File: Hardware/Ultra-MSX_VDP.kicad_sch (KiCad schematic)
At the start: 4 parts, among them J3 Ultra-VDP-daughter

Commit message: Started fixing many small issues.
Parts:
- added C12: C_GRM21BR71A106KA73K, Capacitor_SMD:C_0805_2012Metric_Pad1.18x1.45mm_HandSolder, symbol LRJ-parts:C_GRM21BR71A106KA73K
- added J12: Amphenol_L77HDE15SOL2, LRJ:Amphenol_L77HDE15SOL2, symbol LRJ-parts:Amphenol_L77HDE15SOL2
- added J13: Conn_NREC004, Connector_PinHeader_2.54mm:PinHeader_1x06_P2.54mm_Vertical_SMD_Pin1Right, symbol LRJ-parts:Conn_NREC006
- added R43: R_ERJ-3GEYJ105V, Resistor_SMD:R_0603_1608Metric, symbol LRJ-parts:R_ERJ-3GEYJ105V
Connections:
- net GNDA is gone; now on net GND: J3.47
- net +5V: now also C12.1, J12.9 (DC_5V)
- net BOUT: now also J12.3 (BLUE)
- net GND: now also C12.2, J12.10 (Sync_Ret/GND), J12.5 (GNDD), J12.6 (GNDr), J12.7 (GNDg), J12.8 (GNDb), J13.6 (Pin_6), R43.1
- net GOUT: now also J12.2 (GREEN)
- net HSYNC: now also J12.13 (HSync)
- net ROUT: now also J12.1 (RED)
- net TCK_VDP: now also J13.2 (Pin_2)
- net TDI_VDP: now also J13.3 (Pin_3)
- net TDO_VDP: now also J13.1 (Pin_1)
- net TMS_VDP: now also J13.4 (Pin_4)
- net VSYNC: now also J12.14 (VSync)
- new net: J12.11, J12.12, J12.15, J12.SH, R43.2
- new net +3.3V: J13.5 (Pin_5)
- new net VID_ID: J12.4 (ID_Bit2)
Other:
- note added: "Addressing"
- note added: "Clocks VDP"
- note added: "Data Bus"
- note added: "JTAG"
- note added: "JTAG connector"
- note added: "Only used with an F18A VDP."
- note added: "Video Signals"
- note removed: "Memory-suggestions: ----------------------- Modern ---- IS42S16100H IS45S16100H Legacy ----"
- note removed: "Off-limits names ---- Headers: J1 J2 J3 J4 J5 J6 J7 J11 Chips: U3 U6 U14 Crystals: Y1 Y3 Caps: C1 C2 C3 C9 C10 C11 C12 C13 C14 C15 C16 C73 Resistors: R12 R16 R17"
- note removed: "VTO - voltage Controlled Oscillator -------- Frequencies needed: 25.175 MHz 4.43361875 MHz 3.579545 MHz"

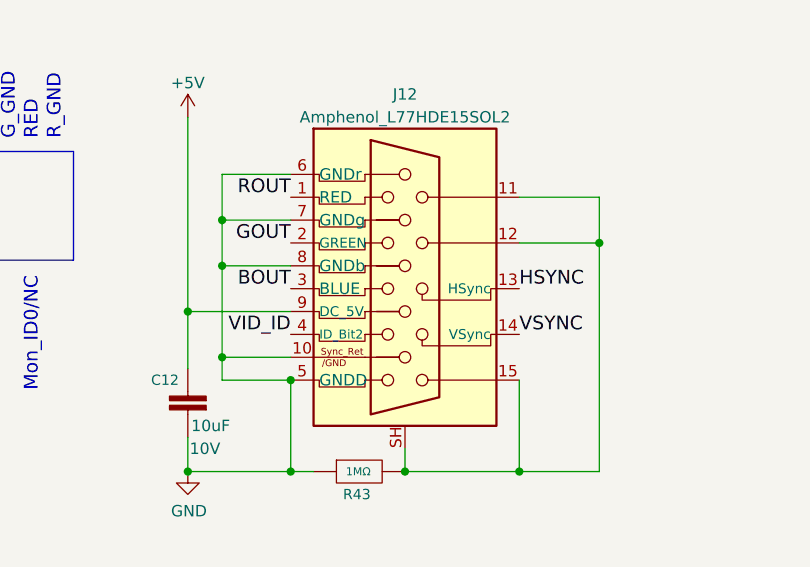
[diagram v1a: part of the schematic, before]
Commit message: Updated the readme, silenced multiple errors in Kicad regarding simulation-files.
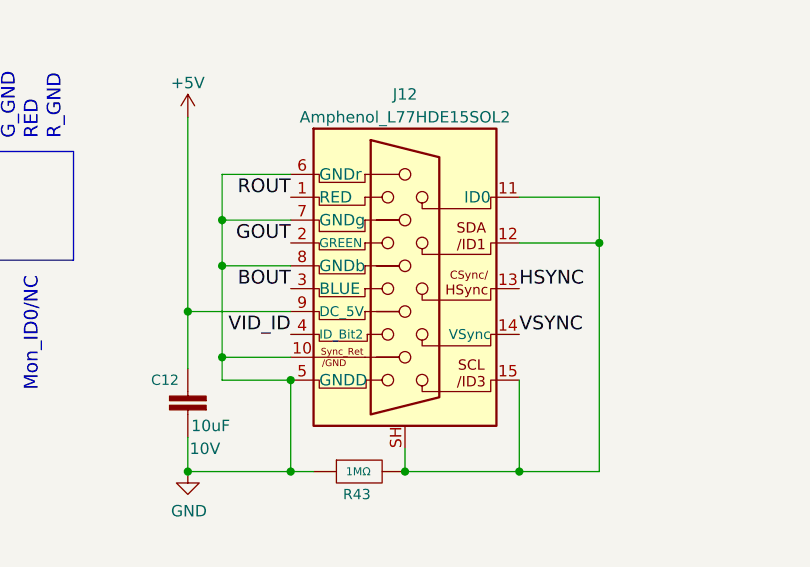
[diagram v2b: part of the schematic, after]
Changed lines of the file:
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@@
+      (effects (font (size 1.27 1.27)) hide)
+    )
+    (property "Sim.Enable" "0" (at 314.96 44.45 0)
       (effects (font (size 1.27 1.27)) hide)
     )
@@
     )
     (property "Datasheet" "~" (at 53.467 38.608 0)
+      (effects (font (size 1.27 1.27)) hide)
+    )
+    (property "Sim.Enable" "0" (at 53.34 91.44 0)
       (effects (font (size 1.27 1.27)) hide)
     )
@@
       (effects (font (size 1.27 1.27)) hide)
     )
+    (property "Sim.Enable" "0" (at 120.65 59.69 0)
+      (effects (font (size 1.27 1.27)) hide)
+    )

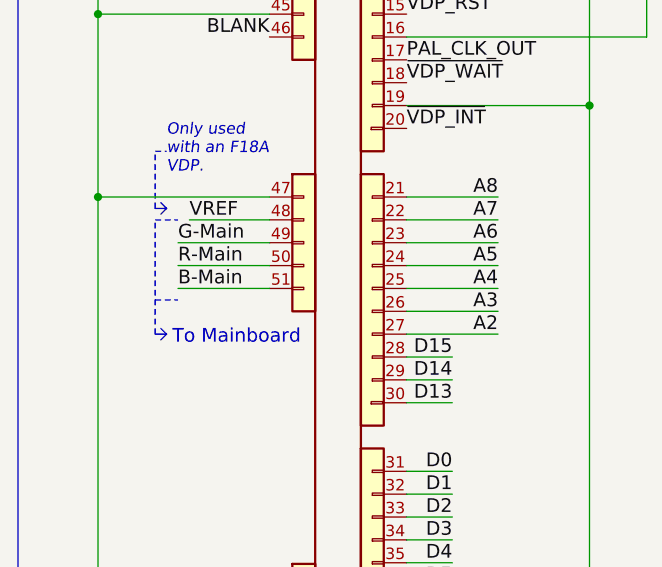
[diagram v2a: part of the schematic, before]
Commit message: Many tweaks and changes, such as a slight redesign of the VDP-baord.
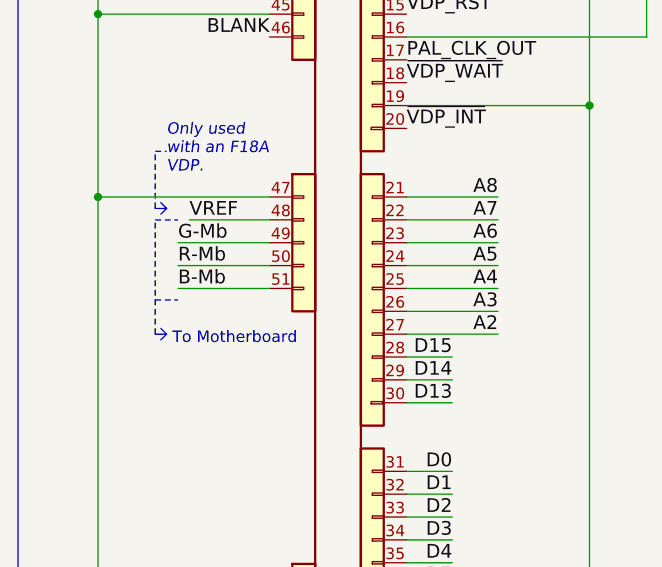
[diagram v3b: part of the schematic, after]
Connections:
- net B-Main: no longer J3.51
- net G-Main: no longer J3.49
- net R-Main: no longer J3.50
- new net B-Mb: J3.51
- new net G-Mb: J3.49
- new net R-Mb: J3.50
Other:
- note added: "To Motherboard"
- note removed: "To Mainboard"
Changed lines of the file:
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@@
     (effects (font (size 1.524 1.524) (thickness 0.3048) bold) (justify right bottom))
   )
-  (text "To Mainboard" (at 34.925 113.03 0)
-    (effects (font (size 1.524 1.524)) (justify left bottom))
+  (text "To Motherboard" (at 34.925 113.03 0)
+    (effects (font (size 1.27 1.27)) (justify left bottom))
   )
   (text "GND" (at 254 27.94 90)
@@
     (effects (font (size 1.524 1.524)) (justify right bottom))
   )
-  (label "B-Main" (at 35.56 106.68 0) (fields_autoplaced)
+  (label "B-Mb" (at 35.56 106.68 0) (fields_autoplaced)
     (effects (font (size 1.524 1.524)) (justify left bottom))
   )
@@
     (effects (font (size 1.524 1.524)) (justify left bottom))
   )
+  (label "NTSC_CLKO" (at 378.46 64.77 0) (fields_autoplaced)
+    (effects (font (size 1.524 1.524)) (justify left bottom))
+  )
   (label "D4" (at 66.04 137.16 180) (fields_autoplaced)
     (effects (font (size 1.524 1.524)) (justify right bottom))
@@
     (effects (font (size 1.524 1.524)) (justify right bottom))
   )
-  (label "G-Main" (at 35.56 101.6 0) (fields_autoplaced)
+  (label "G-Mb" (at 35.56 101.6 0) (fields_autoplaced)
     (effects (font (size 1.524 1.524)) (justify left bottom))
   )
@@
     (effects (font (size 1.524 1.524)) (justify left bottom))
   )
-  (label "NTSC_CLKO" (at 378.46 64.77 0) (fields_autoplaced)
-    (effects (font (size 1.524 1.524)) (justify left bottom))
-  )
   (label "VID_ID" (at 382.27 222.25 0) (fields_autoplaced)
     (effects (font (size 1.524 1.524)) (justify left bottom))
@@
     (effects (font (size 1.524 1.524)) (justify right bottom))
   )
-  (label "R-Main" (at 35.56 104.14 0) (fields_autoplaced)
-    (effects (font (size 1.524 1.524)) (justify left bottom))
-  )
+  (label "R-Mb" (at 35.56 104.14 0) (fields_autoplaced)
+    (effects (font (size 1.524 1.524)) (justify left bottom))
+  )

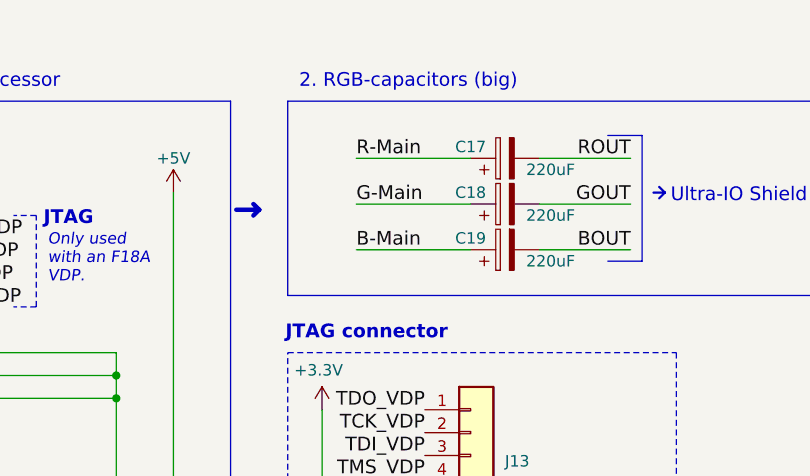
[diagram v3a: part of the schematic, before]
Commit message: Returned to Simm-72 memory module to simplify design, returned to AT40K40 with 254 io, FPGA.
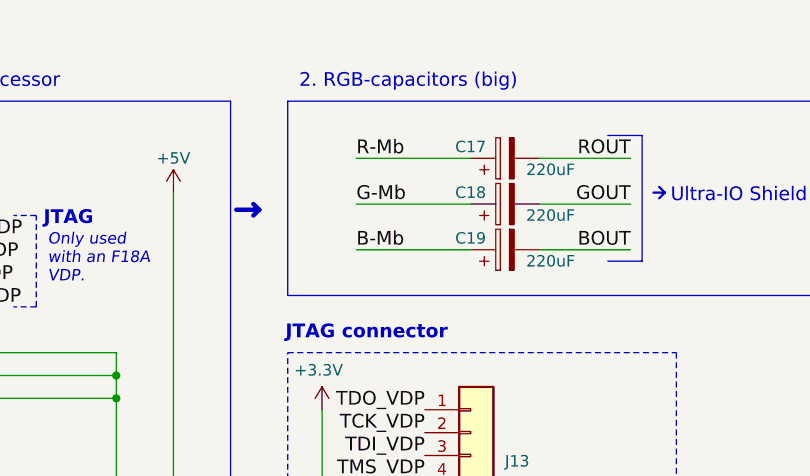
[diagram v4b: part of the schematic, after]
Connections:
- net B-Main is gone; now on net B-Mb: C19.1
- net G-Main is gone; now on net G-Mb: C18.1
- net R-Main is gone; now on net R-Mb: C17.1
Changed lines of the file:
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@@
     (effects (font (size 1.524 1.524)) (justify left bottom))
   )
-  (label "R-Main" (at 107.95 26.67 0) (fields_autoplaced)
+  (label "R-Mb" (at 107.95 26.67 0) (fields_autoplaced)
     (effects (font (size 1.524 1.524)) (justify left bottom))
   )
@@
     (effects (font (size 1.524 1.524)) (justify right bottom))
   )
-  (label "G-Main" (at 107.95 31.75 0) (fields_autoplaced)
+  (label "G-Mb" (at 107.95 31.75 0) (fields_autoplaced)
     (effects (font (size 1.524 1.524)) (justify left bottom))
   )
@@
     (effects (font (size 1.524 1.524)) (justify left bottom))
   )
-  (label "B-Main" (at 107.95 36.83 0) (fields_autoplaced)
-    (effects (font (size 1.524 1.524)) (justify left bottom))
-  )
+  (label "B-Mb" (at 107.95 36.83 0) (fields_autoplaced)
+    (effects (font (size 1.524 1.524)) (justify left bottom))
+  )
